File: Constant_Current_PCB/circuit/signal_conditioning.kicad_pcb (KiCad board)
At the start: 2 copper layers, 37 x 24.5 mm, 7 parts, among them J2 Screw_Terminal_01x03, J3 Screw_Terminal_01x02, Q1 NPN, U3 TL081CP

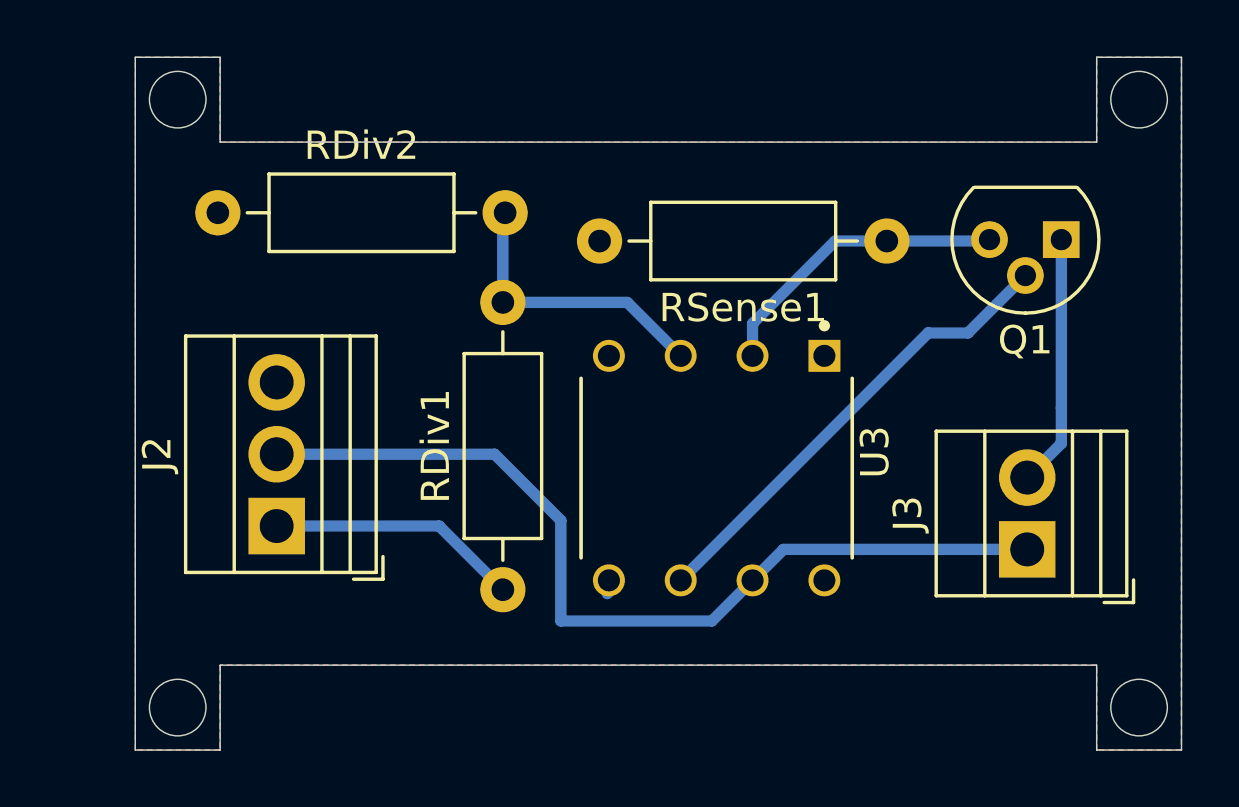
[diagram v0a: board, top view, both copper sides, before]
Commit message: add 3d view - fix img
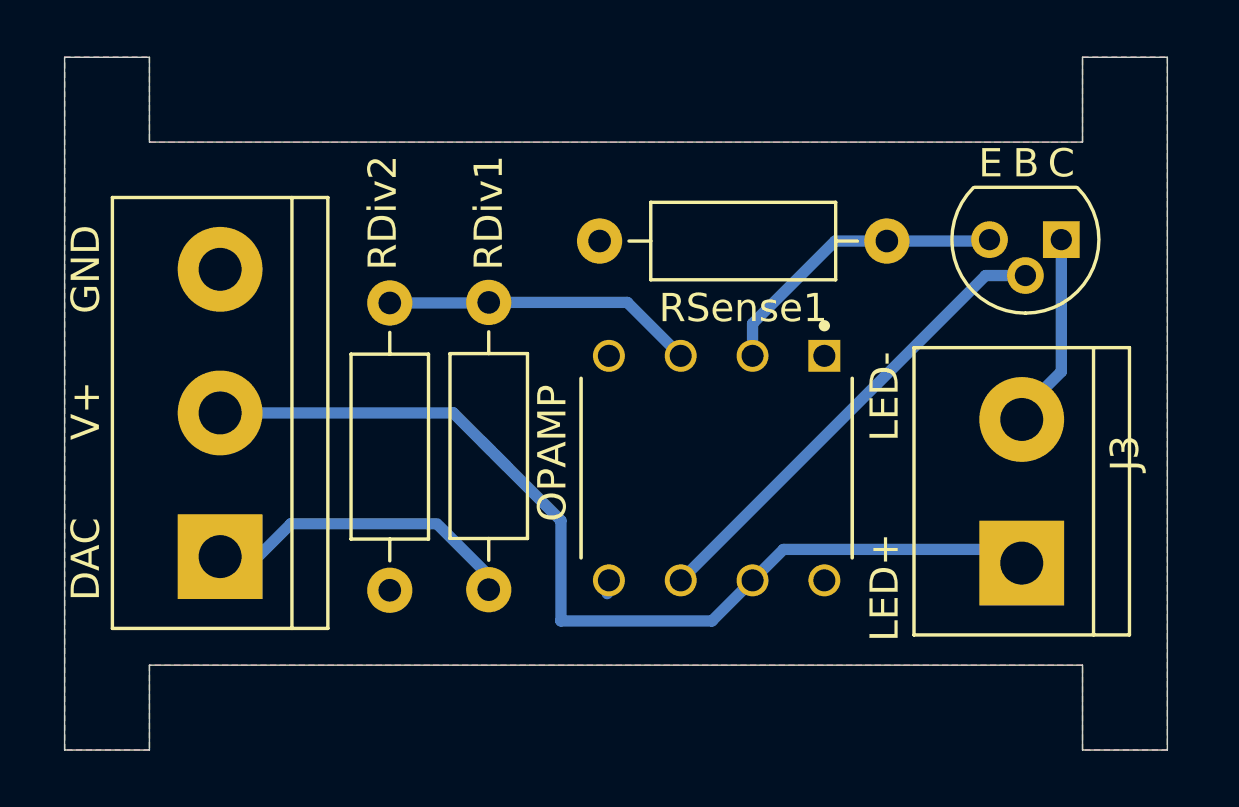
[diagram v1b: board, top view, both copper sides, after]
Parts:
- J2: footprint TerminalBlock:TerminalBlock_Xinya_XY308-2.54-3P_1x03_P2.54mm_Horizontal -> TerminalBlock:TerminalBlock_bornier-3_P5.08mm
- J3: footprint TerminalBlock:TerminalBlock_Xinya_XY308-2.54-2P_1x02_P2.54mm_Horizontal -> TerminalBlock:TerminalBlock_bornier-2_P5.08mm
- moved RDiv2 14.7 mm to (76.0, 68.8), turned to 90 degrees
- moved J2 2.27 mm to (70.0, 67.7)
- moved J3 0.52 mm to (98.3, 67.9)
- moved RDiv1 0.50 mm to (79.5, 68.8)
- renumbered U3 to OPAMP
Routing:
- net LED+: track 32.2 -> 35.8 mm
- net LED-: track 8.91 -> 6.37 mm
- net Net-(J2-Pin_1): track 8.93 -> 11.4 mm
- net Net-(U3-IN_+): track 10.3 -> 10.8 mm
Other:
- board size 37 x 24.5 mm -> 39 x 24.5 mm
- board text added: "B"
- board text added: "C"
- board text added: "DAC"
- board text added: "E"
- board text added: "GND"
- board text added: "LED+"
- board text added: "LED-"
- board text added: "V+"
